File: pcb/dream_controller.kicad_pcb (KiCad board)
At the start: 2 copper layers, 17.8 x 45.7 mm, 4 parts, among them J1 Touchplate, J2 Joystick, U1 Teensy-LC, U2 MCP4922

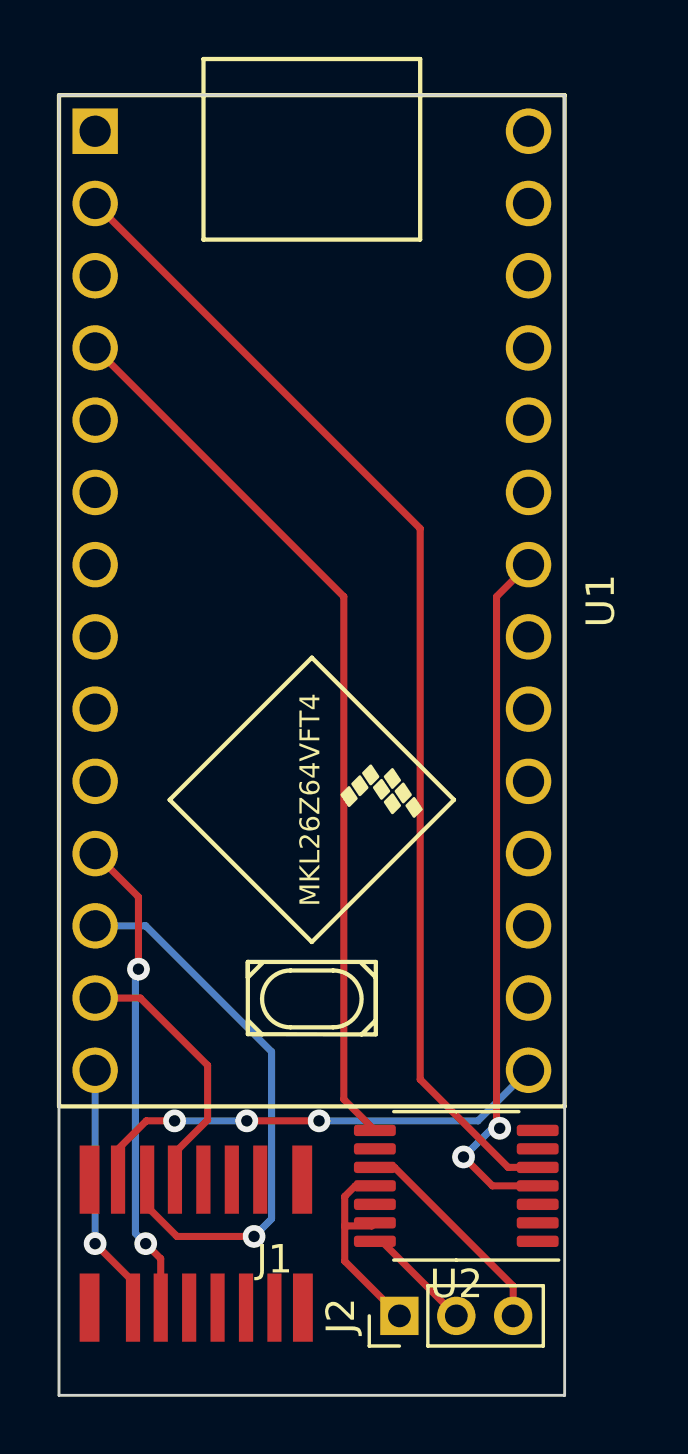
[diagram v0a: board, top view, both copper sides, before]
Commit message: Merge working branch to main (#1)
* Complete schematic

* Cleanup

* Additional cleanup

* silkscreen name

Co-authored-by: ocelot <ocelot@ocelots-Mini.fios-router.home>
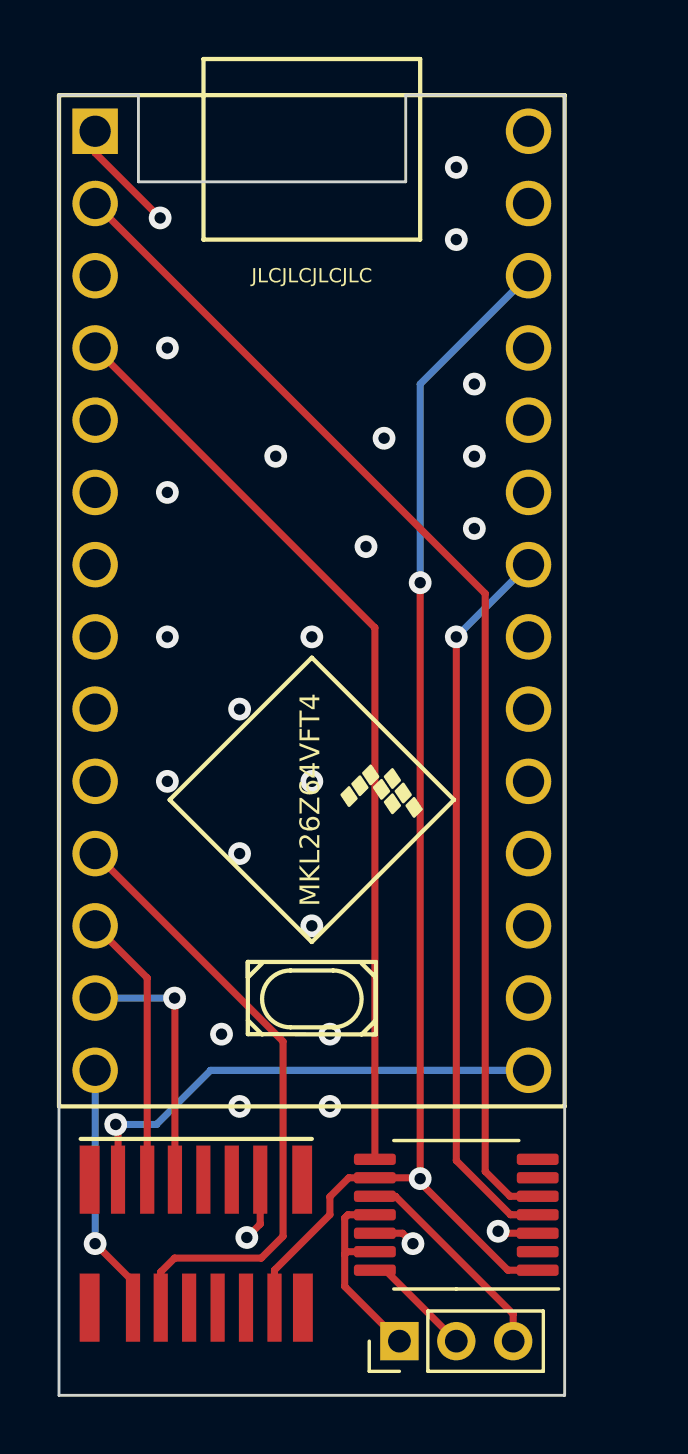
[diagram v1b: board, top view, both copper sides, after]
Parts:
- moved U2 1.02 mm to (139.7, 124.5)
- moved J2 0.89 mm to (137.7, 128.9)
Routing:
- net +3V3: track 0.00 -> 47.0 mm, vias 0 -> 2
- net /CAP_CS: track 19.9 -> 9.68 mm, vias 1 -> 0
- net GND: track 0.00 -> 9.14 mm, vias 0 -> 25
- net /CAP_DR: track 17.0 -> 22.3 mm, vias 2 -> 0
- net /DAC_LATCH: track 31.6 -> 32.6 mm
- net /DAC_DATA: track 40.9 -> 41.9 mm
- net /CAP_CLK: track 16.7 -> 17.3 mm, vias 3 -> 1
- net /DAC_CLK: track 25.1 -> 25.7 mm, vias 2 -> 1
- net /CAP_COPI: track 9.43 -> 9.18 mm, vias 0 -> 1
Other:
- outline, holes or cut-outs redrawn
- board text added: "JLCJLCJLCJLC"
- board text added: "VREF"
- board text added: "X"
- board text added: "Y"
- board text added: "eric halin march 2022 dream-controller v.01"
